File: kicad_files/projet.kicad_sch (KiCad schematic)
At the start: 7 parts, among them Q1 BC817, Q2 BC807, U1 STM32G031K8Tx, U2 MCP4901, U3 LM1117MP-3.3

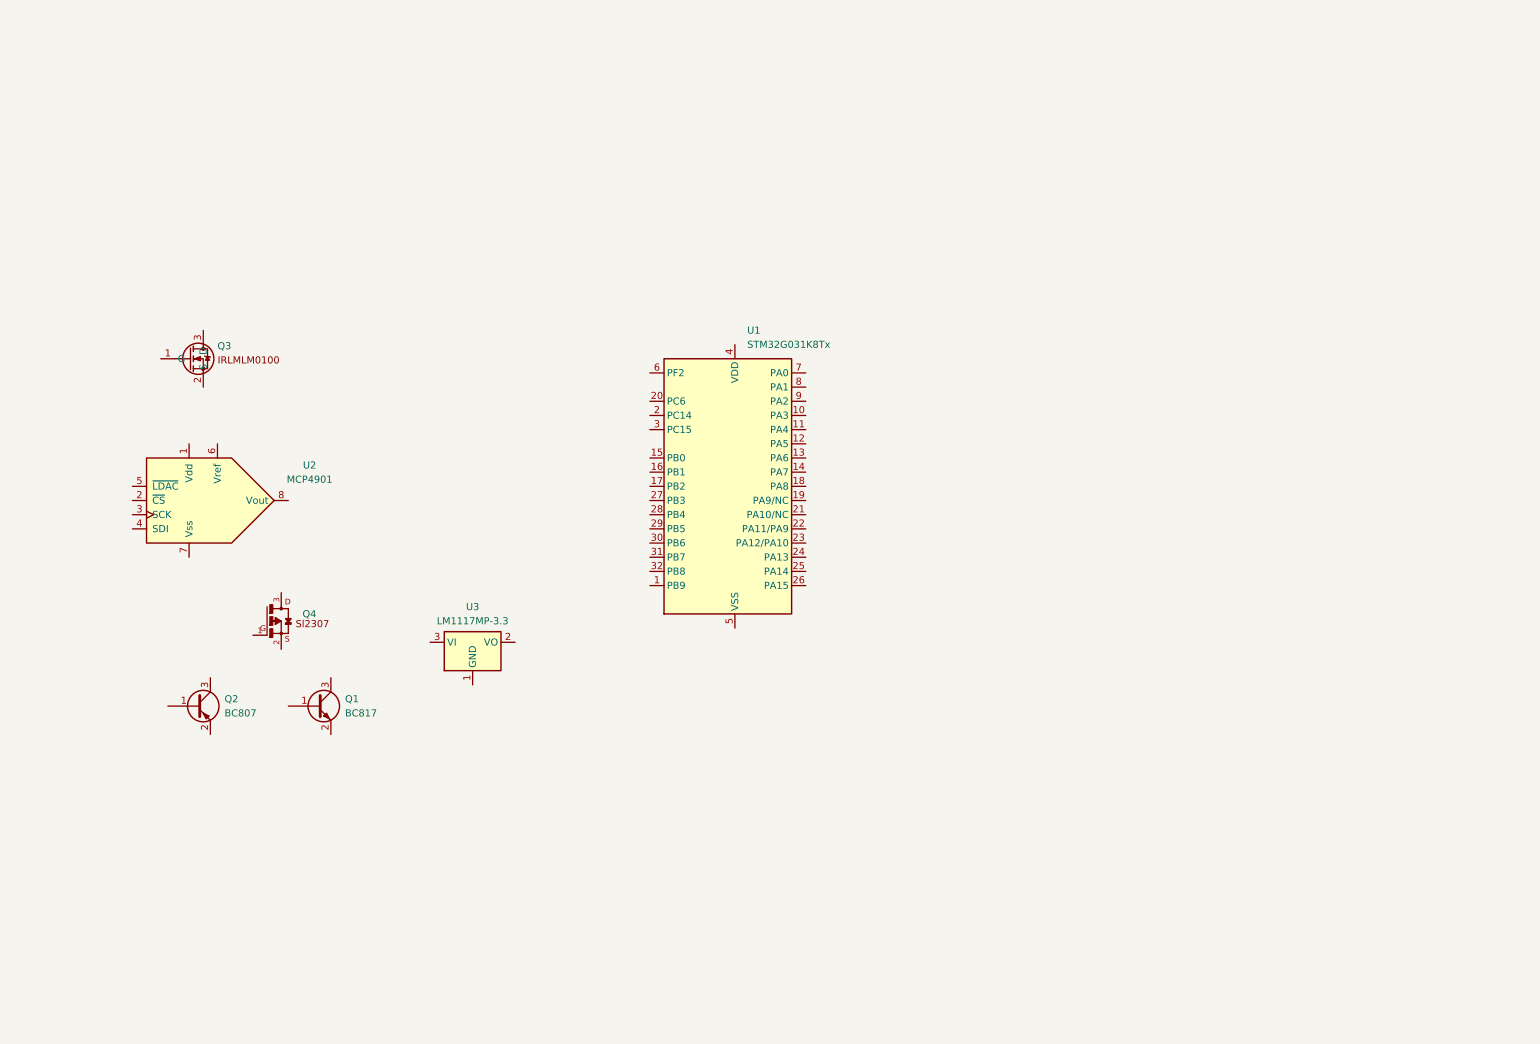
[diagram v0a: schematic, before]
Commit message: code pour le dac et schéma pour amplifier le signal
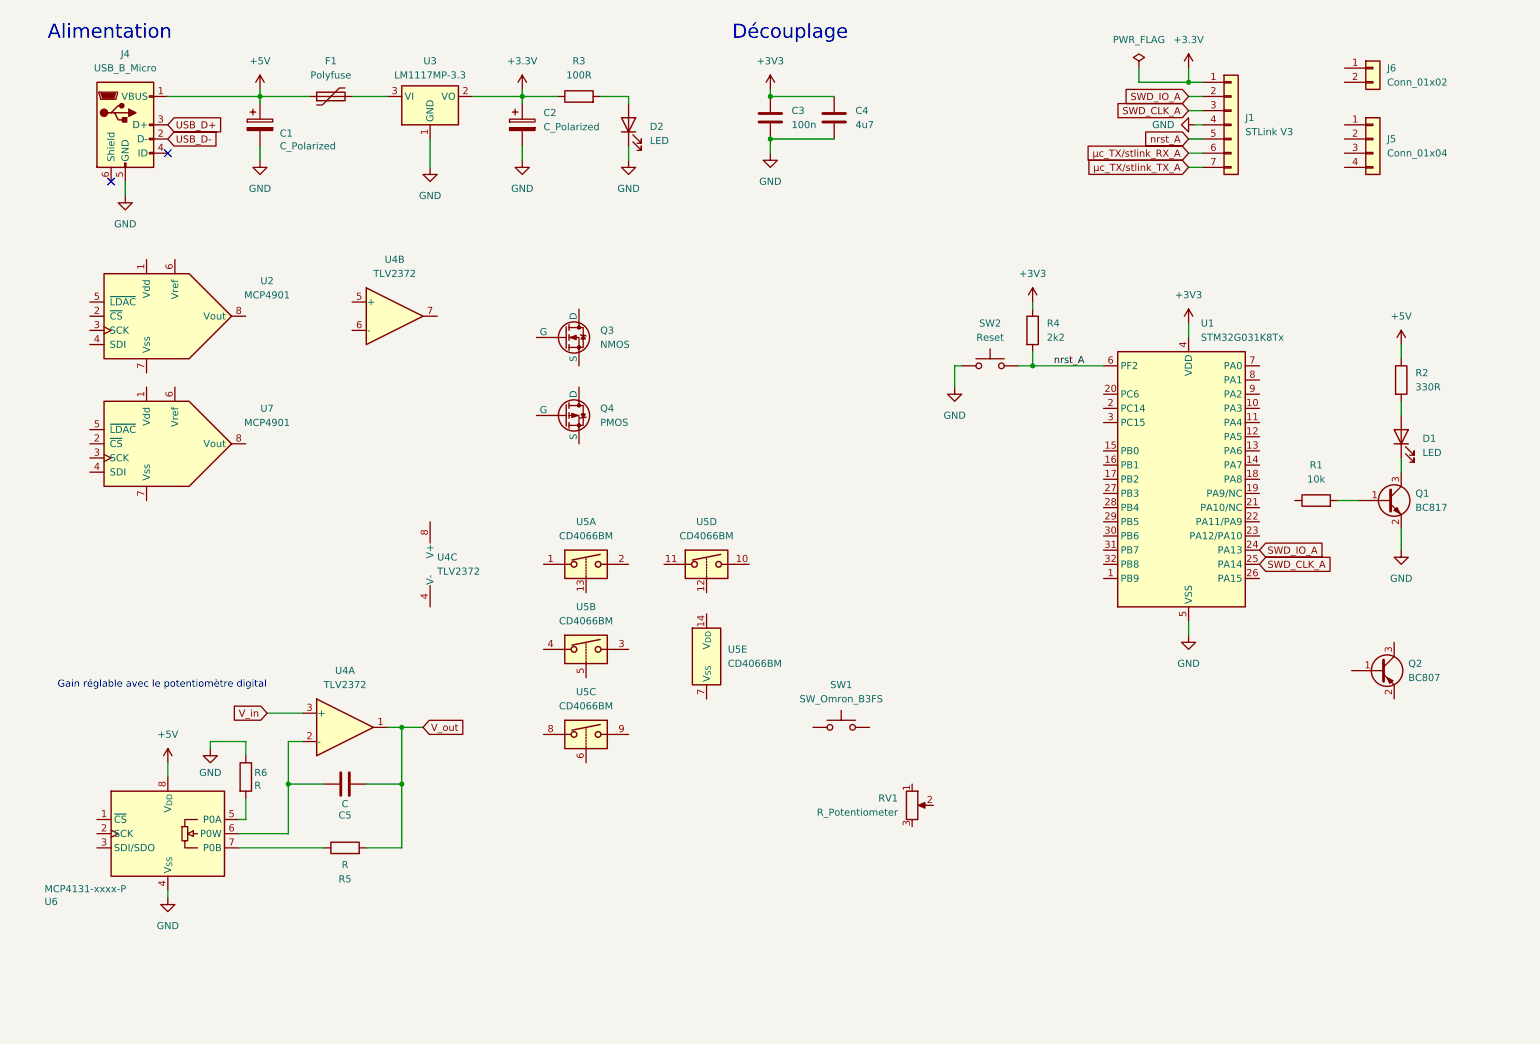
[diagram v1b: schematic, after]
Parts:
- removed Q3: ~, symbol missing_schematics:IRLML0100
- removed Q4: ~, symbol missing_schematics:Sl2307
- added C1, C2: C_Polarized, symbol Device:C_Polarized
- added C3: 100n, symbol Device:C
- added C4: 4u7, symbol Device:C
- added C5: C, symbol Device:C
- added D1, D2: LED, symbol Device:LED
- added F1: Polyfuse, symbol Device:Polyfuse
- added J1: STLink V3, symbol Connector_Generic:Conn_01x07
- added J4: USB_B_Micro, symbol Connector:USB_B_Micro
- added J5: Conn_01x04, symbol Connector_Generic:Conn_01x04
- added J6: Conn_01x02, symbol Connector_Generic:Conn_01x02
- added Q3: NMOS, symbol Simulation_SPICE:NMOS
- added Q4: PMOS, symbol Simulation_SPICE:PMOS
- added R1: 10k, symbol Device:R
- added R2: 330R, symbol Device:R
- added R3: 100R, symbol Device:R
- added R4: 2k2, symbol Device:R
- added R5, R6: R, symbol Device:R
- added RV1: R_Potentiometer, symbol Device:R_Potentiometer
- added SW1: SW_Omron_B3FS, symbol Switch:SW_Omron_B3FS
- added SW2: Reset, symbol Switch:SW_Omron_B3FS
- added U4: TLV2372, symbol Amplifier_Operational:TLV2372
- added U5: CD4066BM, Package_SO:SO-14_3.9x8.65mm_P1.27mm, symbol Analog_Switch:CD4066BM
- added U6: MCP4131-xxxx-P, Package_DIP:DIP-8_W7.62mm, symbol Potentiometer_Digital:MCP4131-xxxx-P
- added U7: MCP4901, symbol Analog_DAC:MCP4901
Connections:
- net SWD_IO_A: now reaches U1.24 (PA13)
- net SWD_IO_A: now also J1.2 (Pin_2)
- net SWD_CLK_A: now reaches U1.25 (PA14)
- net SWD_CLK_A: now also J1.3 (Pin_3)
- net +3V3: now reaches U1.4 (VDD)
- net +3V3: now also C3.1, C4.1, R4.1
- net GND: now reaches U1.5 (VSS)
- net GND: now also Q1.2 (E), U3.1 (GND), C1.2, C2.2, C3.2, C4.2, D2.1 (K), J1.4 (Pin_4), J4.5 (GND), R6.1, SW2.1, U6.4 (V_{SS})
- net nrst_A: now reaches U1.6 (PF2)
- net nrst_A: now also J1.5 (Pin_5), R4.2, SW2.2
- net at Q1.1 (B): now also R1.2
- net at Q1.3 (C): now also D1.1 (K)
- net +3.3V: now reaches U3.2 (VO)
- net +3.3V: now also C2.1, J1.1 (Pin_1), R3.1
- net at U3.3 (VI): now also F1.2
- new net: R6.2, U6.5 (P0A)
- new net: D1.2 (A), R2.2
- new net: R5.1, U6.7 (P0B)
- new net: D2.2 (A), R3.2
- new net: C5.1, U4.2 (-), U6.6 (P0W)
- new net +5V: C1.1, F1.1, J4.1 (VBUS), R2.1, U6.8 (V_{DD})
- new net USB_D+: J4.3 (D+)
- new net USB_D-: J4.2 (D-)
- new net V_in: U4.3 (+)
- new net V_out: C5.2, R5.2, U4.1
- new net µc_TX/stlink_RX_A: J1.6 (Pin_6)
- new net µc_TX/stlink_TX_A: J1.7 (Pin_7)
- no-connect marks 0 -> 2
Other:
- note added: "Alimentation"
- note added: "Découplage"
- note added: "Gain réglable avec le potentiomètre digital"
- moved on the sheet: Q1, Q2, U1, U2, U3

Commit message: circuit
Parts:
- removed C5: C, symbol Device:C
- removed D1: LED, symbol Device:LED
- removed R1: 10k, symbol Device:R
- removed R2: 330R, symbol Device:R
- removed R6: R, symbol Device:R
- added C10: 22u, symbol Device:C
- added C11: C, symbol Device:C
- added C12, C6, C8: 10u, symbol Device:C
- added C13: 6.8u, symbol Device:C
- added C14, C7, C9: 0.1u, symbol Device:C
- added D3, D4, D5, D6: LED, symbol Device:LED
- added R10, R11, R8, R9: 330R, symbol Device:R
- added R12, R13: 10k, symbol Device:R
- added R7: 100R, symbol Device:R
- C1, C2: value C_Polarized -> 10u
- R4: value 2k2 -> 10k
- R5: value R -> 10k
- RV1: value R_Potentiometer -> 10k
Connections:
- net V_in is gone; now on an unnamed net: U4.3 (+)
- net +3.3V: now also R7.2
- net +3V3: now also R5.1, R12.1, R13.1
- net +5V: now also U2.1 (Vdd), U2.6 (Vref), U4.8 (V+), U5.1, U5.11, U5.14 (V_{DD}), U5.4, U5.8, U7.1 (Vdd), U7.6 (Vref), C11.1, C12.1, C13.1, C14.1, C6.1, C7.1, C8.1, C9.1; no longer U6.8 (V_{DD})
- net GND: now also RV1.1, SW1.2, U2.7 (Vss), U4.4 (V-), U5.7 (V_{SS}), U7.7 (Vss), C10.2, C12.2; no longer C3.2, C4.2, Q1.2 (E), U6.4 (V_{SS})
- net µc_TX/stlink_RX_A: now also U1.23 (PA12/PA10)
- net µc_TX/stlink_TX_A: now also U1.1 (PB9)
- net at SW1.1: now also R5.2, U1.11 (PA4)
- net at U6.7 (P0B): no longer R5.1
- net at U1.10 (PA3): now also RV1.2
- net SPI1_SCK: now reaches U1.8 (PA1)
- net SPI1_SCK: now also U2.3 (SCK), U7.3 (SCK), R12.2
- net SPI1_MOSI: now reaches U1.9 (PA2)
- net SPI1_MOSI: now also U2.4 (SDI), U7.4 (SDI), R13.2
- net at U6.6 (P0W): no longer U4.2 (-)
- net at RV1.3: now also C10.1, R7.1
- net at U4.5 (+): now also U7.8 (Vout)
- net Vout_2: now reaches U4.6 (-)
- net Vout_2: now also U4.7
- net /CS_DAC1: now reaches U2.2 (~{CS})
- net at U5.3: now also R9.1
- net at U5.2: now also R8.1
- net at U5.10: now also R11.1
- net at U5.9: now also R10.1
- net /CS_DAC2: now reaches U7.2 (~{CS})
- net V_out renamed Vout_1
- net Vout_1: now also U4.2 (-); no longer R5.2
- new net: D3.2 (A), R8.2
- new net: D4.2 (A), R9.2
- new net: D6.2 (A), R11.2
- new net: D5.2 (A), R10.2
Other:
- note added: "bande passante: 3MHz"
- note added: "f_coupure = 72Hz"
- note removed: "Alimentation"
- note removed: "Découplage"
- note removed: "Gain réglable avec le potentiomètre digital"
- moved on the sheet: C3, C4, Q1, Q2, Q3, Q4, R4, RV1, SW1, SW2, U1, U2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

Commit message: circuit
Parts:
- added C15, C5: 0.1u, symbol Device:C
- added R1, R2: 100k, symbol Device:R
- added U8: MCP4131, Package_DIP:DIP-8_W7.62mm, symbol Potentiometer_Digital:MCP4131-xxxx-P
- U6: value MCP4131-xxxx-P -> MCP4131
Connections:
- net +5V: now also U6.8 (V_{DD}), C15.1, C5.1, U8.8 (V_{DD})
- net GND: now also U4.3 (+), U4.5 (+), U6.4 (V_{SS}), U8.4 (V_{SS})
- net Vout_1: now also J6.1 (Pin_1), U6.6 (P0W); no longer U4.2 (-)
- net Vout_2: now also J6.2 (Pin_2), U8.6 (P0W); no longer U4.6 (-)
- net /CS_DAC1: now also U1.28 (PB4)
- net /CS_DAC2: now also U1.29 (PB5)
- net /CS_POT1: now reaches U1.12 (PA5)
- net /CS_POT1: now also U6.1 (~{CS})
- net /CS_POT2: now reaches U1.13 (PA6)
- net /CS_POT2: now also U8.1 (~{CS})
- net SW_1: now reaches U1.15 (PB0)
- net SW_1: now also U5.13
- net SW_2: now reaches U1.16 (PB1)
- net SW_2: now also U5.5
- net SW_3: now reaches U1.17 (PB2)
- net SW_3: now also U5.6
- net SW_4: now reaches U1.27 (PB3)
- net SW_4: now also U5.12
- net SPI2_MOSI: now reaches U1.31 (PB7)
- net SPI2_MOSI: now also U6.3 (SDI/SDO), U8.3 (SDI/SDO)
- net SPI2_SCK: now reaches U1.32 (PB8)
- net SPI2_SCK: now also U6.2 (SCK), U8.2 (SCK)
- net at U2.8 (Vout): now also R2.1; no longer U4.3 (+)
- net at U7.8 (Vout): now also R1.1; no longer U4.5 (+)
- net at U6.7 (P0B): now also U4.2 (-), R2.2
- new net: R1.2, U4.6 (-), U8.7 (P0B)
- no-connect marks 2 -> 13
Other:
- note removed: "bande passante: 3MHz"
- moved on the sheet: C10, C11, C12, C13, C14, C3, C4, C6, C7, C8, C9, D3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

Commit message: schema et datasheets
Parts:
- removed D5, D6: LED, symbol Device:LED
- removed Q2: BC807, Package_TO_SOT_SMD:SOT-23, symbol Transistor_BJT:BC807
- removed R5: 10k, symbol Device:R
- removed R7: 100R, symbol Device:R
- removed SW1: SW_Omron_B3FS, symbol Switch:SW_Omron_B3FS
- removed U7: MCP4901, symbol Analog_DAC:MCP4901
- removed U8: MCP4131, Package_DIP:DIP-8_W7.62mm, symbol Potentiometer_Digital:MCP4131-xxxx-P
- added D1, D7: LED, symbol Device:LED
- added Q2, Q5, Q6: BC817, Package_TO_SOT_SMD:SOT-23, symbol Transistor_BJT:BC817
- added R14, R6: 2k2, symbol Device:R
- added R15: 330R, symbol Device:R
- added R16, R17: 10k, symbol Device:R
- added SW3, SW4, SW5: SW_Omron_B3FS, symbol Switch:SW_Omron_B3FS
- added U7: MCP4131, Package_DIP:DIP-8_W7.62mm, symbol Potentiometer_Digital:MCP4131-xxxx-P
- C10: value 22u -> 18n
- C11: value C -> 0.1u
- C12: value 10u -> 0.1u
- C15: value 0.1u -> 47n
- C2: value 10u -> 100u
- C5, C9: value 0.1u -> C
- C8: value 10u -> C
- R1: value 100k -> 330R
- R10, R8: value 330R -> 2k2
- R2: value 100k -> 10k
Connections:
- net +3.3V: now also C11.2, C12.1, C6.1, C7.1, RV1.1, U2.1 (Vdd), U2.6 (Vref), U6.8 (V_{DD}), U7.8 (V_{DD})
- net +3V3: now also R2.1, R16.1; no longer R12.1, R13.1
- net +5V: now also D3.2 (A), D4.2 (A), F1.2, U3.3 (VI), D1.2 (A), D7.2 (A); no longer C11.1, C12.1, C15.1, C5.1, C6.1, C7.1, C8.1, C9.1, F1.1, J4.1 (VBUS), U2.1 (Vdd), U2.6 (Vref), U5.1, U5.11, U5.14 (V_{DD}), U5.4, U5.8, U6.8 (V_{DD})
- net GND: no longer C1.2, C10.2, C12.2, C2.2, D2.1 (K), J4.5 (GND), RV1.1, SW2.1, U1.5 (VSS), U2.7 (Vss), U3.1 (GND), U4.3 (+), U4.4 (V-), U4.5 (+), U5.7 (V_{SS}), U6.4 (V_{SS})
- net SPI1_MOSI: no longer R13.2, U1.9 (PA2)
- net SPI1_SCK: no longer R12.2, U1.8 (PA1)
- net SWD_CLK_A: no longer U1.25 (PA14)
- net SWD_IO_A: no longer U1.24 (PA13)
- net nrst_A: no longer R4.2
- net µc_TX/stlink_RX_A: no longer U1.23 (PA12/PA10)
- net µc_TX/stlink_TX_A: no longer U1.1 (PB9)
- net at R1.2: now also D1.1 (K); no longer U4.6 (-)
- net OUTPUT: now reaches C15.2
- net OUTPUT: now also U4.6 (-), U4.7
- net at U1.10 (PA3): no longer RV1.2
- net at U5.2: no longer R8.1
- net LED3: now reaches R8.2
- net LED3: no longer D3.2 (A)
- net at C10.1: no longer RV1.3
- net at D3.1 (K): now also R9.2
- net at U6.5 (P0A): now also U4.1, U4.2 (-), U6.6 (P0W)
- net at D4.1 (K): now also R11.2
- net at U2.8 (Vout): now also U4.3 (+); no longer R2.1
- net at R11.1: now also Q6.3 (C); no longer U5.10
- net at R9.1: now also Q2.3 (C); no longer U5.3
- net at Q1.1 (B): now also R6.1
- net at Q1.3 (C): now also R1.1
- net at R10.1: now also Q6.1 (B); no longer U5.9
- net LED4: now reaches R10.2
- net SPI2_MOSI: no longer names the net of U6.3 (SDI/SDO)
- net SPI2_MOSI: no longer U1.31 (PB7)
- net SPI2_SCK: no longer names the net of U6.2 (SCK)
- net SPI2_SCK: no longer U1.32 (PB8)
- net SW_1: no longer names the net of U1.15 (PB0)
- net SW_1: no longer U5.13
- net SW_2: no longer names the net of U1.16 (PB1)
- net SW_2: no longer U5.5
- net SW_3: no longer names the net of U1.17 (PB2)
- net SW_3: no longer U5.6
- net SW_4: no longer names the net of U1.27 (PB3)
- net SW_4: no longer U5.12
- removed net Vout_1: J6.1 (Pin_1), U4.1, U6.6 (P0W)
- net Vout_2: no longer names the net of J6.2 (Pin_2)
- net Vout_2: no longer U4.7
- net /CS_DAC1: no longer names the net of U1.28 (PB4)
- net /CS_DAC1: no longer U2.2 (~{CS})
- net /CS_DAC2: no longer names the net of U1.29 (PB5)
- net /CS_POT1: no longer names the net of U6.1 (~{CS})
- net /CS_POT1: no longer U1.12 (PA5)
- net /CS_POT2: no longer names the net of U1.13 (PA6)
- new net: R13.2, R2.2, SW3.1
- new net: R16.2, R17.2, SW5.1
- new net: C15.1, U6.7 (P0B), U7.5 (P0A), U7.6 (P0W)
- new net: C10.2, U4.5 (+), U7.7 (P0B)
- new net: R12.2, R4.2, SW4.1
- new net: Q5.3 (C), R15.1
- new net: D7.1 (K), R15.2
- new net: Q5.1 (B), R14.1
- new net: Q2.1 (B), R8.1
- new net: F1.1, J4.1 (VBUS)
- new net LED1: R6.2
- new net LED2: R14.2
- new net POT1: RV1.2
- new net SWITCH1: C5.1, R13.1
- new net SWITCH2: C8.1, R12.1
- new net SWITCH3: C9.1, R17.1
- new net /CS_DAC: U2.2 (~{CS})
- no-connect marks 13 -> 2
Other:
- note removed: "f_coupure = 72Hz"
- moved on the sheet: C1, C13, C14, C2, C3, C4, C6, C7, D2, J4, Q1, R3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

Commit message: schéma avec filtre, ao gain et suiveur
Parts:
- added C16, C17: C, symbol Device:C
- added C18: 0.1u, symbol Device:C
- added C19: 6.8u, symbol Device:C
- added R5: R, symbol Device:R
- C10: value 18n -> C
- C15: value 47n -> C
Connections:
- net +3.3V: now also U5.14 (V_{DD}), C18.1, C19.1
- net at U6.5 (P0A), U6.6 (P0W): now also U2.8 (Vout); no longer U4.1, U4.2 (-)
- net at U7.5 (P0A), U7.6 (P0W): now also U4.2 (-), R5.1; no longer C15.1, U6.7 (P0B)
- net at C10.1: now also U5.2
- net at U4.5 (+), U7.7 (P0B): now also U4.1; no longer C10.2
- net at U4.3 (+): now also U5.1, U5.11, U5.4, U5.8, U6.7 (P0B); no longer U2.8 (Vout)
- net at U5.3: now also C15.1
- net SW2: now reaches U5.5
- net SW1: now reaches U5.13
- net at U5.10: now also C17.1
- net SW4: now reaches U5.12
- net SW3: now reaches U5.6
- net at U5.9: now also C16.1
- net OUTPUT renamed SORTIE
- net SORTIE: no longer C15.2
- net SWITCH1 renamed BT1
- net SWITCH2 renamed BT2
- net SWITCH3 renamed BT3
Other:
- moved on the sheet: C11, C12, C6, C7, U2, U4A, U4B, U5A, U5E, U6, U7

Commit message: simulation ok
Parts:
- removed C12: 0.1u, symbol Device:C
- removed U7: MCP4131, Package_DIP:DIP-8_W7.62mm, symbol Potentiometer_Digital:MCP4131-xxxx-P
- added RV2: R_Potentiometer, symbol Device:R_Potentiometer
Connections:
- net at R5.1, U4.2 (-): now also RV2.2, RV2.3
- net at U4.1, U4.5 (+): now also RV2.1

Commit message: circuit kicad
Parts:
- removed J5: Conn_01x04, symbol Connector_Generic:Conn_01x04
- removed J6: Conn_01x02, symbol Connector_Generic:Conn_01x02
- removed RV1: 10k, symbol Device:R_Potentiometer
- added C12: C, symbol Device:C
- added C20: 6.8u, symbol Device:C
- added C21: 0.1u, symbol Device:C
- added J2: Sortie, symbol Connector_Generic:Conn_01x01
- added R18, R19, R20, R7: R, symbol Device:R
- added U7: TLV2372, symbol Amplifier_Operational:TLV2372
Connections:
- net +5V: now also C20.1, C21.1, U7.8 (V+)
- net SORTIE_FILTRE: now reaches U5.1, U5.11, U5.4, U5.8, U6.7 (P0B)
- net SORTIE_FILTRE: now also R7.1; no longer U4.3 (+)
- net SORTIE: no longer names the net of U4.6 (-), U4.7
- net SORTIE: now also J2.1 (Pin_1)
- new net: C12.1, R19.2
- new net: R20.1, U4.3 (+), U7.1
- new net: R18.2, R7.2, U7.3 (+)
- new net: R19.1, R20.2, U7.2 (-)
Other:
- moved on the sheet: C1, C10, C11, C13, C14, C15, C16, C17, C18, C19, C2, C5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

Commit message: circuit
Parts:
- removed unit 2 of U5
- removed unit 1 of U5
- removed unit 4 of U5
- removed unit 3 of U5
- added Q10, Q7, Q8, Q9: IRLML0030, Package_TO_SOT_SMD:SOT-23, symbol Transistor_FET:IRLML0030
- added R21, R22, R23, R24: 10k, symbol Device:R
- C5, C8, C9: value C -> 1u
- R3: value 100R -> 330R
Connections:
- net BT1: now also U1.11 (PA4)
- net BT2: now also U1.12 (PA5)
- net BT3: now also U1.13 (PA6)
- net LED1: now also U1.29 (PB5)
- net LED2: now also U1.30 (PB6)
- net LED3: now also U1.31 (PB7)
- net LED4: now also U1.32 (PB8)
- net SORTIE_FILTRE: now also Q10.3 (D), Q7.3 (D), Q8.3 (D), Q9.3 (D)
- net SPI1_MOSI: now also U1.23 (PA12/PA10), U6.3 (SDI/SDO)
- net SPI1_SCK: now also U1.27 (PB3), U6.2 (SCK)
- net SW1: now also Q7.1 (G), R21.1
- net SW2: now also Q8.1 (G), R22.1
- net SW3: now also Q9.1 (G), R23.1
- net SW4: now also Q10.1 (G), R24.1
- net SWD_CLK_A: now also U1.25 (PA14)
- net SWD_IO_A: now also U1.24 (PA13)
- net /CS_DAC: now also U1.15 (PB0)
- net µc_TX/stlink_RX_A: now also U1.10 (PA3)
- net µc_TX/stlink_TX_A: now also U1.9 (PA2)
- net /CS_POT: now reaches U6.1 (~{CS})
- net /CS_POT: now also U1.16 (PB1)
- net at C16.1: now also Q9.2 (S)
- net at C15.1: now also Q8.2 (S)
- net at C10.1: now also Q7.2 (S)
- net at C17.1: now also Q10.2 (S)
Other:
- moved on the sheet: C10, C12, C15, C16, C17, D1, D3, D4, D7, J2, Q1, Q2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
